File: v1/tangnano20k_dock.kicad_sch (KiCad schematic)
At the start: 41 parts, among them J1 Mini-DIN-6, J2 2x20 Pin Female, J3 Conn_01x03_Male, J4 Conn_01x20, J5 Conn_01x02, J6 RCA, J7 FCR684205T, J8 AudioJack3, U1 TXS0104E, U2 TangNano20K, U3 CS4354

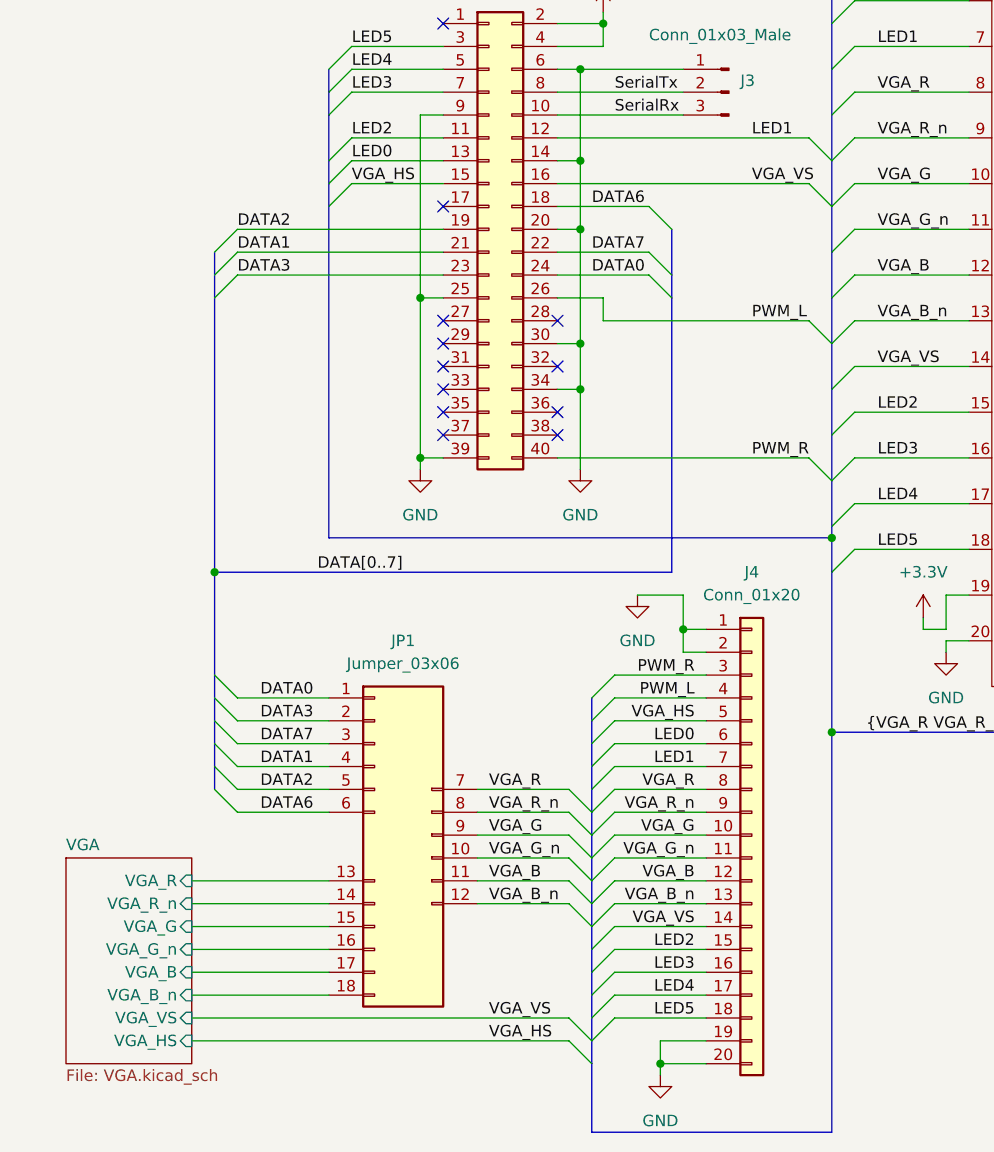
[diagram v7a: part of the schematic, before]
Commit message: Updated VGA jumper block from 3x6 to 3x8
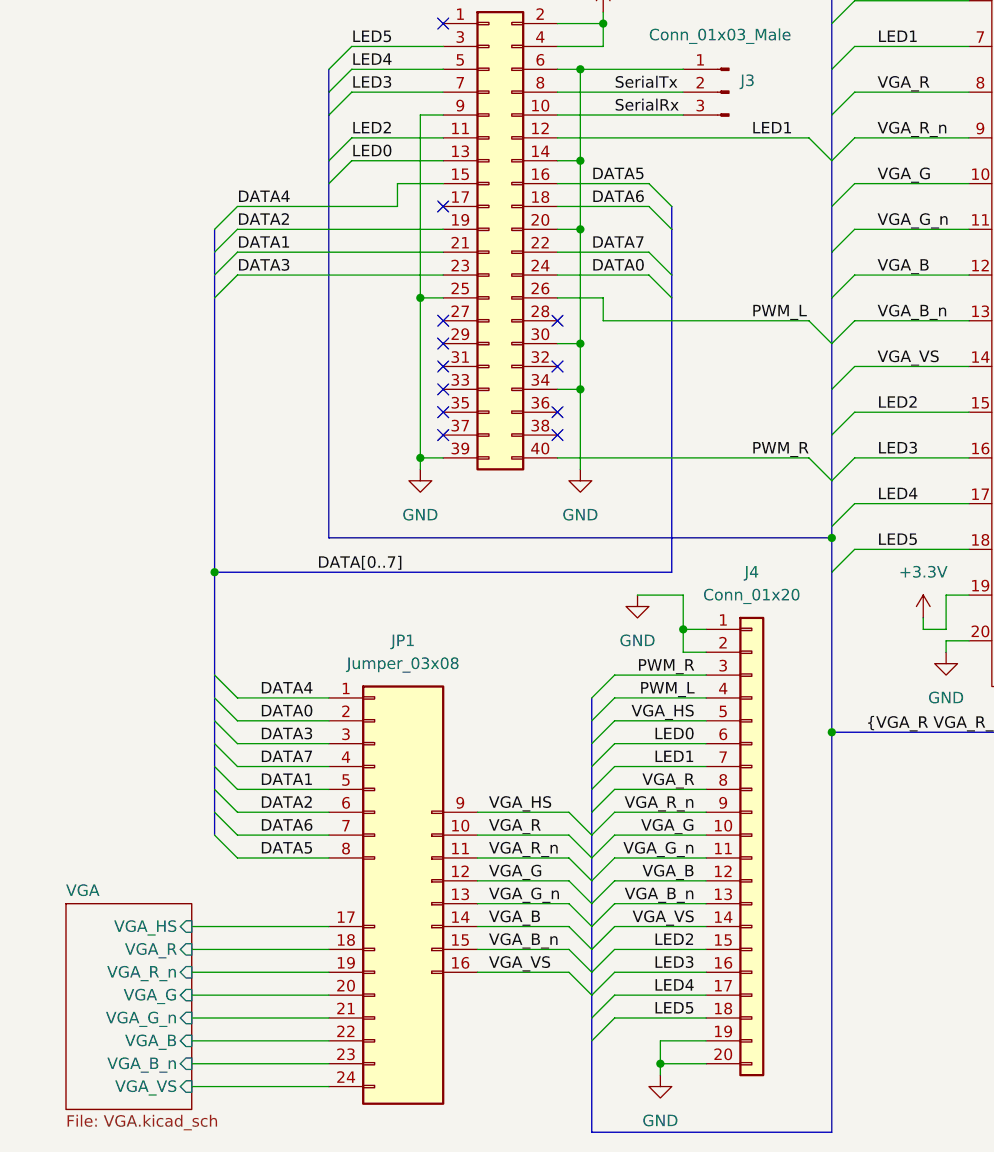
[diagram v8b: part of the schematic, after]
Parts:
- removed JP1: Jumper_03x06, TangNano20k:PinHeader_3x06_P2.54mm_Vertical, symbol TangNano20k:Jumper_03x06
- added JP1: Jumper_03x08, TangNano20k:PinHeader_3x08_P2.54mm_Vertical, symbol TangNano20k:Jumper_03x08
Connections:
- net DATA0: now also JP1.2 (Pin_2)
- net DATA1: now also JP1.5 (Pin_5)
- net DATA2: now also JP1.6 (Pin_6)
- net DATA3: now also JP1.3 (Pin_3)
- net DATA6: now also JP1.7 (Pin_7)
- net DATA7: now also JP1.4 (Pin_4)
- net VGA/VGA_B: now also JP1.22 (Pin_22)
- net VGA/VGA_B_n: now also JP1.23 (Pin_23)
- net VGA/VGA_G: now also JP1.20 (Pin_20)
- net VGA/VGA_G_n: now also JP1.21 (Pin_21)
- net VGA/VGA_R: now also JP1.18 (Pin_18)
- net VGA/VGA_R_n: now also JP1.19 (Pin_19)
- net VGA_B: now also JP1.14 (Pin_14)
- net VGA_B_n: now also JP1.15 (Pin_15)
- net VGA_G: now also JP1.12 (Pin_12)
- net VGA_G_n: now also JP1.13 (Pin_13)
- net VGA_HS: now also JP1.9 (Pin_9); no longer J2.15 (Pin_15)
- net VGA_R: now also JP1.10 (Pin_10)
- net VGA_R_n: now also JP1.11 (Pin_11)
- net VGA_VS: now also JP1.16 (Pin_16); no longer J2.16 (Pin_16)
- new net DATA4: J2.15 (Pin_15), JP1.1 (Pin_1)
- new net DATA5: J2.16 (Pin_16), JP1.8 (Pin_8)
- new net VGA/VGA_HS: JP1.17 (Pin_17)
- new net VGA/VGA_VS: JP1.24 (Pin_24)
